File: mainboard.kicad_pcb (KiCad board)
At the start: 2 copper layers, 142 x 78 mm, 37 parts, among them J1 Raspi Pi Zero 2W, J10 USBDataBoard, J11 DM, J2 LCD, J3 Keyboard, J4 USB Power, J5 Conn_02x20_Odd_Even, J6 Conn_02x20_Odd_Even, J7 DP, J8 USBDataPi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

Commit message: v0.2
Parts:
- added R4: 5.1k, Resistor_SMD:R_0805_2012Metric_Pad1.20x1.40mm_HandSolder, F.Cu at (208.6, 75.5)
- added R5: 5.1k, Resistor_SMD:R_0805_2012Metric_Pad1.20x1.40mm_HandSolder, F.Cu at (208.6, 78.3)
- J5: value Conn_02x20_Odd_Even -> Board
- J6: value Conn_02x20_Odd_Even -> Pi
- U1: footprint Package_SO:SOIC-28W_7.5x17.9mm_P1.27mm -> Package_SO:TSSOP-28_8x9.7mm_P0.65mm
- moved J6 2.00 mm to (134.9, 106.9)
- moved J10 1.20 mm to (210.4, 117.2)
- moved J8 0.80 mm to (216.9, 117.2)
- moved U1 0.25 mm to (95.9, 95.4)
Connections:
- J4 pad A5: unconnected-(J4-PadA5) -> Net-(J4-PadA5)
- J4 pad B5: unconnected-(J4-PadB5) -> Net-(J4-PadB5)
- U3 pad 10: GND -> +3V3
- U4 pad 10: GND -> +3V3
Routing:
- net +3V3: track 96.3 -> 100.9 mm
- net /KB8: track 17.9 -> 21.6 mm
- net Net-(J4-PadB5): track 0.00 -> 3.61 mm
- net Net-(J4-PadA5): track 0.00 -> 3.42 mm
- net /KB9: track 18.4 -> 21.6 mm
- net /KB7: track 19.2 -> 22.1 mm
- net /KB10: track 19.9 -> 22.2 mm
- net /KB6: track 20.4 -> 22.7 mm
- net Net-(J10-Pad2): track 8.50 -> 6.30 mm
- net Net-(J10-Pad1): track 8.50 -> 6.30 mm
- net /Pi Bridge/BR_9: track 9.07 -> 11.1 mm
- net /Pi Bridge/BR_8: track 9.07 -> 11.1 mm
- net /Pi Bridge/BR_7: track 9.07 -> 11.1 mm
- net /Pi Bridge/BR_6: track 9.04 -> 11.0 mm
- net /Pi Bridge/BR_5: track 9.07 -> 11.1 mm
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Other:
- outline, holes or cut-outs redrawn
- board text added: "Cyberpi Mainboard v0.2"
- board text removed: "Cyberpi Mainboard v0.1"

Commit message: updating footprint
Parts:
- J5: value Board -> Conn_02x20_Odd_Even
- J6: value Pi -> Conn_02x20_Odd_Even
- U1: footprint Package_SO:TSSOP-28_8x9.7mm_P0.65mm -> Package_SO:TSSOP-28_6.1x9.7mm_P0.65mm
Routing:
- net +3V3: track 100.9 -> 98.0 mm
- net /KB13: track 23.7 -> 24.7 mm
- net /KB9: track 21.6 -> 22.6 mm
- net /KB8: track 21.6 -> 22.5 mm
- net /KB7: track 22.1 -> 23.1 mm
- net /KB6: track 22.7 -> 23.6 mm
- net /KB5: track 23.2 -> 24.1 mm
- net /KB4: track 23.7 -> 24.7 mm
- net /KB3: track 24.3 -> 25.2 mm
- net /KB2: track 24.8 -> 25.7 mm
- net /KB16: track 25.3 -> 26.3 mm
- net /KB15: track 24.8 -> 25.7 mm
- net /KB14: track 24.3 -> 25.2 mm
- net /KB12: track 23.2 -> 24.2 mm
- net /KB11: track 22.7 -> 23.6 mm
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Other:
- board text added: "Cyberpi Mainboard v0.3"
- board text removed: "Cyberpi Mainboard v0.2"

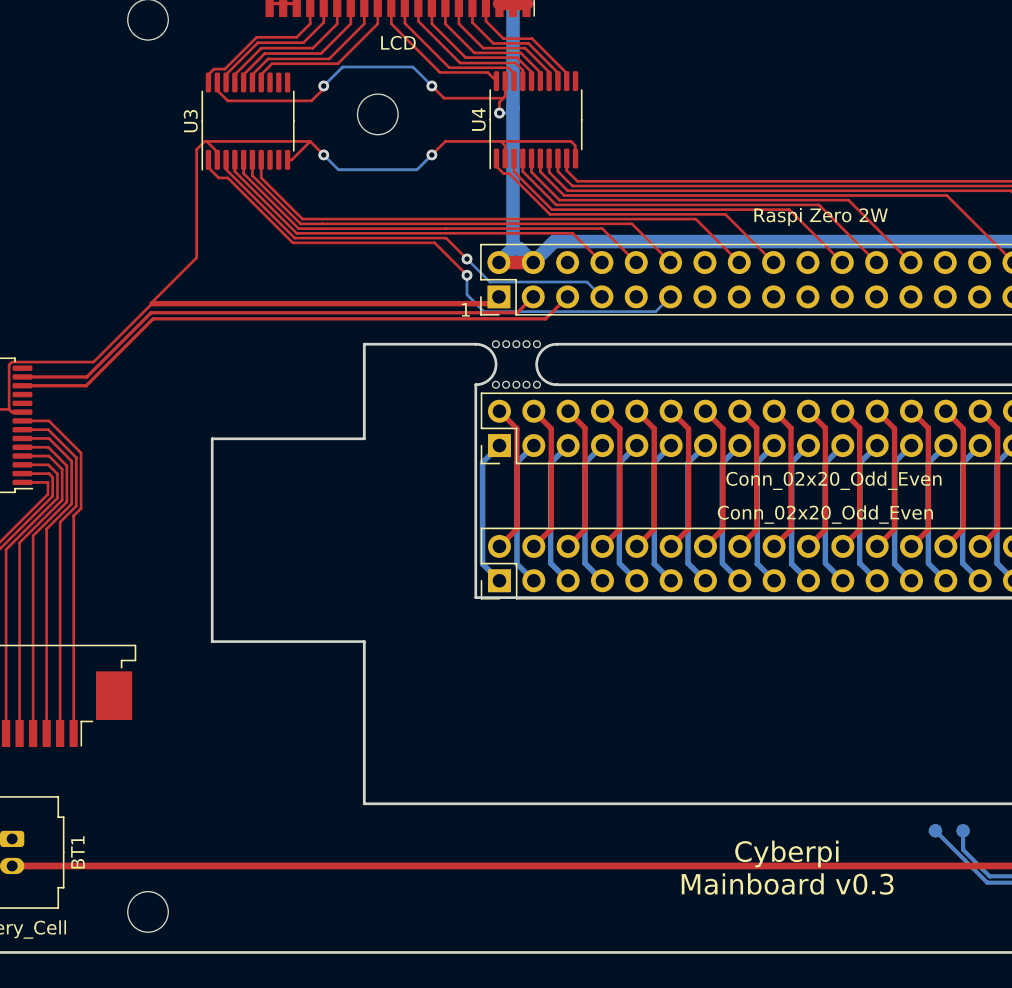
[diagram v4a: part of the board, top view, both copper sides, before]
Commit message: adding bypass caps to level shifter
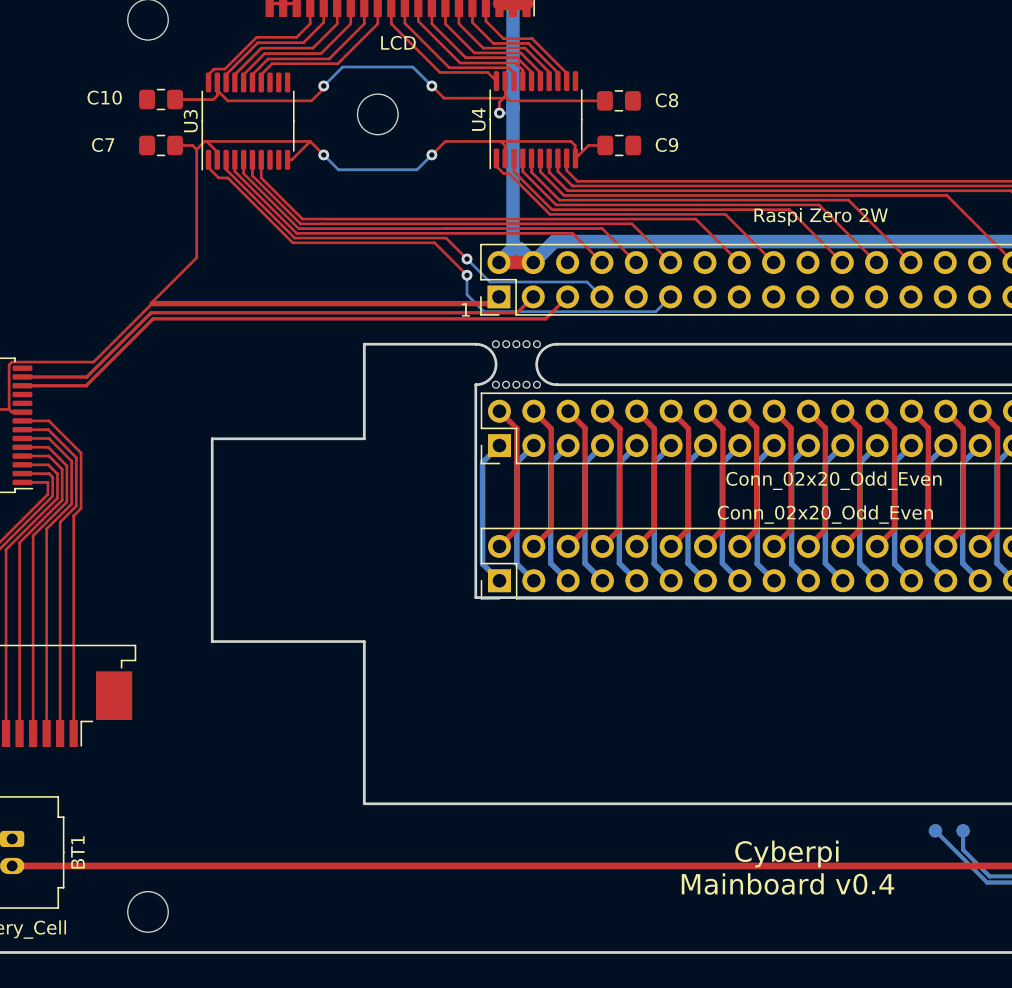
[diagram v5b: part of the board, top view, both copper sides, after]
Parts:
- added C10: 0.1uF 16V, Capacitor_SMD:C_0805_2012Metric_Pad1.18x1.45mm_HandSolder, F.Cu at (109.8, 71.3)
- added C7: 0.1uF 16V, Capacitor_SMD:C_0805_2012Metric_Pad1.18x1.45mm_HandSolder, F.Cu at (109.8, 74.7)
- added C8: 0.1uF 16V, Capacitor_SMD:C_0805_2012Metric_Pad1.18x1.45mm_HandSolder, F.Cu at (143.7, 71.4)
- added C9: 0.1uF 16V, Capacitor_SMD:C_0805_2012Metric_Pad1.18x1.45mm_HandSolder, F.Cu at (143.7, 74.7)
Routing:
- net +5V: track 161.4 -> 173.1 mm
- net +3V3: track 98.0 -> 102.3 mm
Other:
- board text added: "Cyberpi Mainboard v0.4"
- board text removed: "Cyberpi Mainboard v0.3"
